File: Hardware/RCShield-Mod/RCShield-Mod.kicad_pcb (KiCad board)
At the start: 2 copper layers, 13 parts, among them K1 PPM_OUT, P1 ANALOG_EXT, P2 DIGI_EXT, P7 Vinput

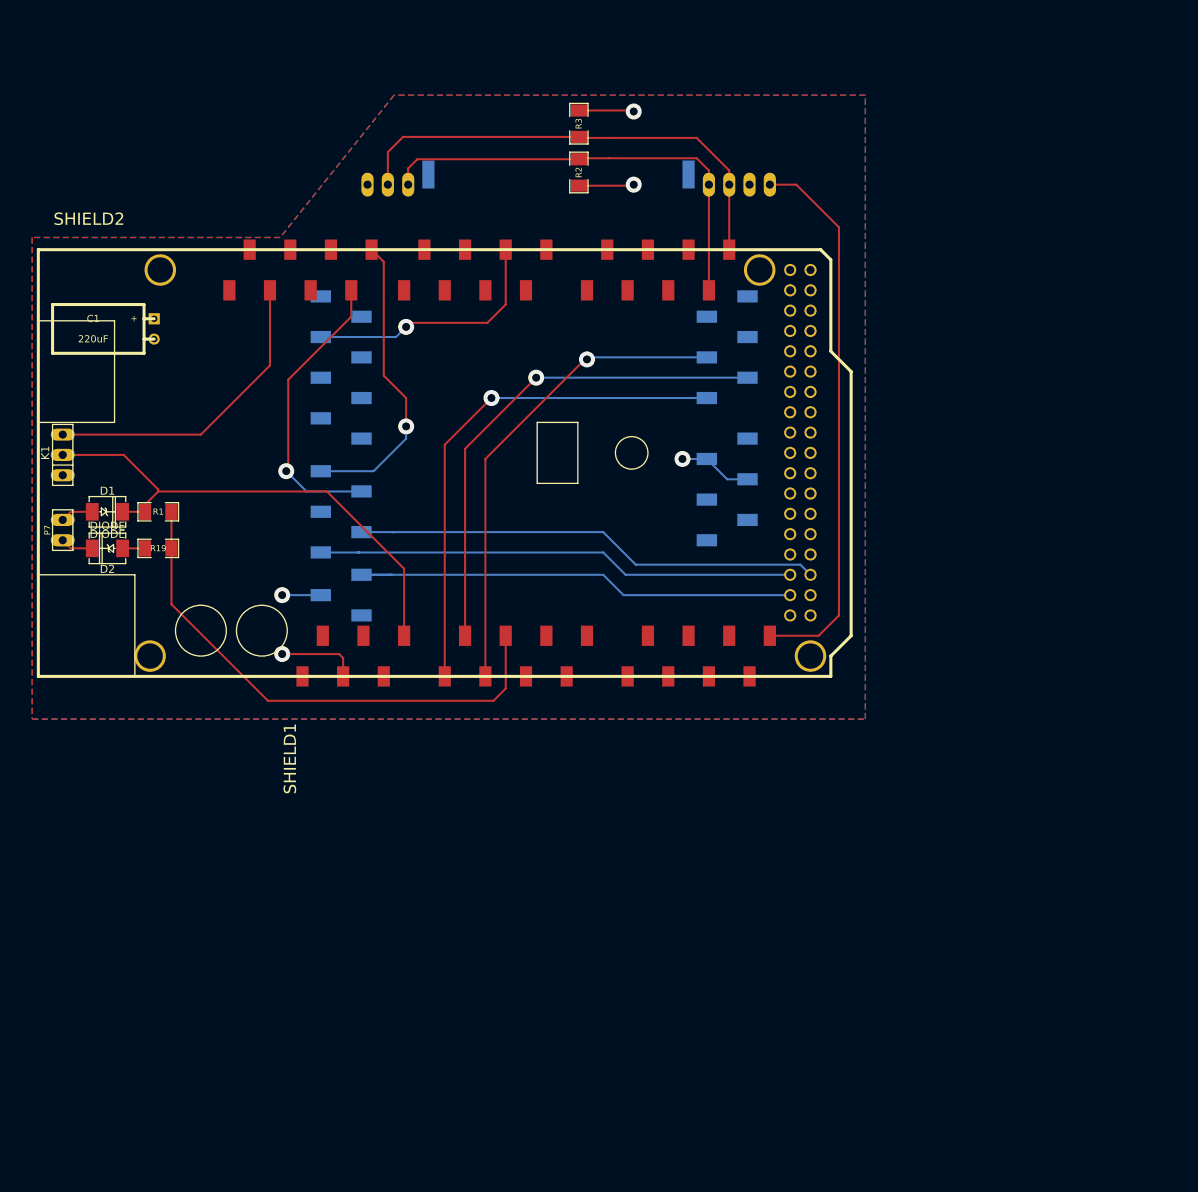
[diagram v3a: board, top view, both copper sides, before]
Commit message: * Updating PCB to more rectangular + Caps + On/Off Switch * Disabling Digital Breakout board for now
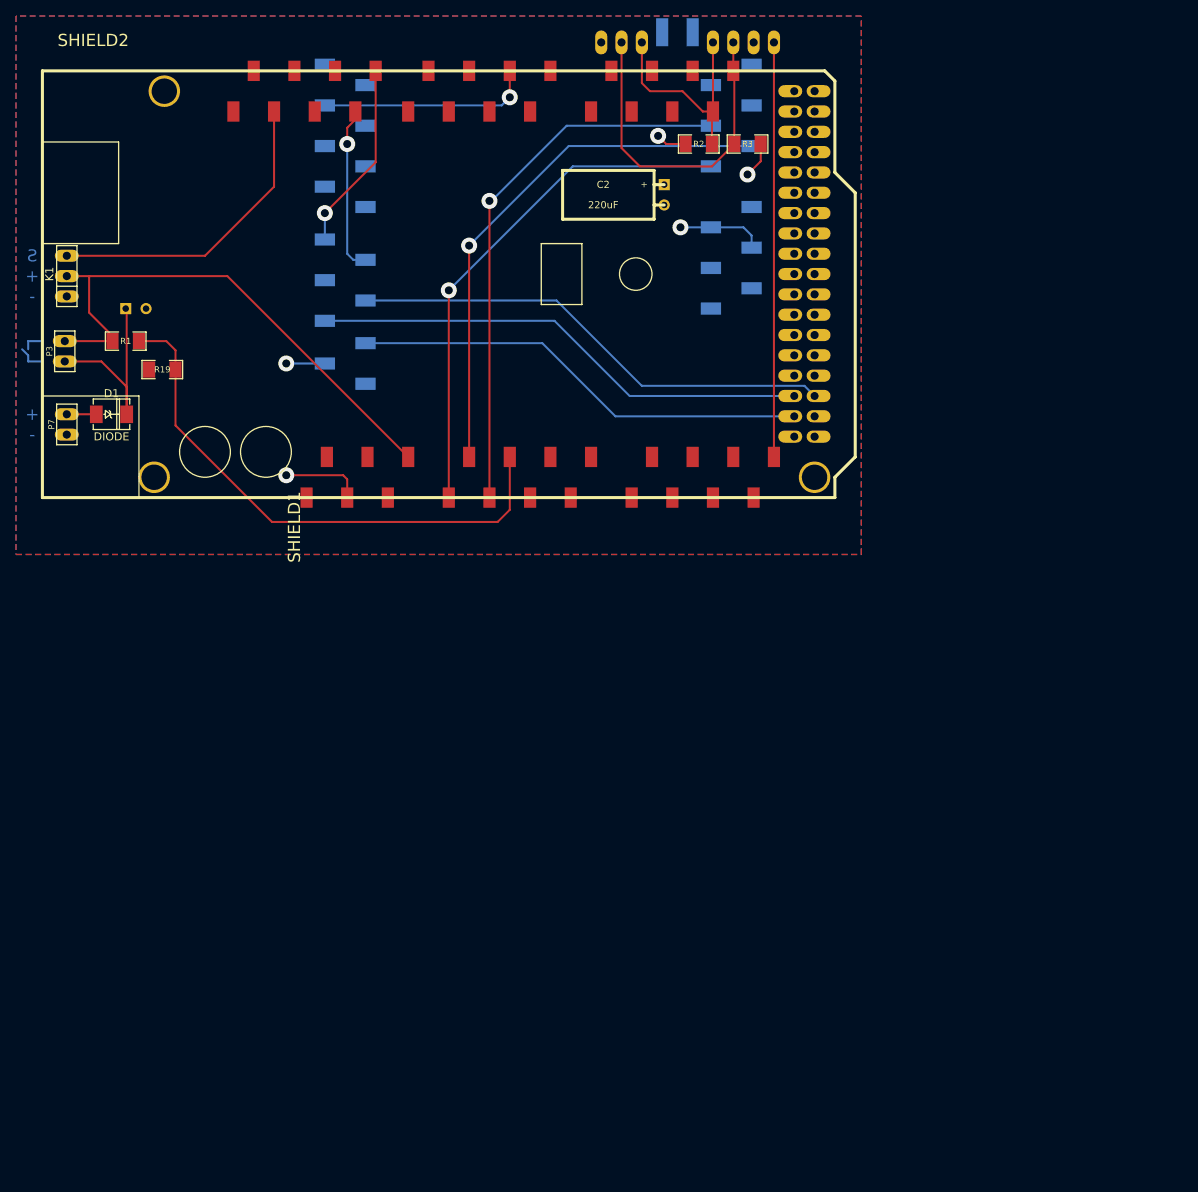
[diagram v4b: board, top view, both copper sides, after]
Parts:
- removed D2: DIODE, DO-214AC(SMA)
- added C2: 220uF, C1V5H, F.Cu at (102.9, 42.9)
- added P3: Vswitch, PIN_ARRAY_2X1_BIG, F.Cu at (27.9, 62.5)
- C1: value 220uF -> 1000uF; moved to B.Cu
- moved P1 34.2 mm to (98.8, 23.9)
- moved SHIELD1 29.0 mm to (113.8, 90.2)
- moved K1 22.4 mm to (28.2, 53.1)
- moved R19 22.4 mm to (40.1, 64.8)
- moved SHIELD2 22.4 mm to (25.1, 80.8)
- moved R1 21.7 mm to (35.6, 61.2)
- moved R3 21.2 mm to (113.3, 36.6), turned to 180 degrees
- moved P2 17.8 mm to (111.5, 23.9)
- moved R2 15.4 mm to (107.2, 36.6), turned to 0 degrees
- moved P7 13.2 mm to (28.2, 71.6)
- moved D1 12.2 mm to (33.8, 70.4)
- moved C1 3.42 mm to (36.8, 57.1), turned to 0 degrees
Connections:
- C1 pad 1: +5V -> Valways
- D1 pad 2: VIN -> Valways
- P7 pad 1: N-0000017 -> GND
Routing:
- net SDA: track 55.8 -> 28.2 mm
- net Valways: track 0.00 -> 25.7 mm
- net DIGI_INT: track 69.0 -> 51.8 mm
- net SCL: track 59.2 -> 42.2 mm
- net SDSEL: track 36.4 -> 20.8 mm
- net GPUSEL: track 37.8 -> 23.7 mm
- net ACCZ: track 60.1 -> 68.7 mm
- net (no net): track 0.00 -> 6.41 mm
- net +5V: track 23.9 -> 18.5 mm
- net DISPINT: track 31.7 -> 26.8 mm
- net ACCY: track 62.4 -> 66.9 mm
- net VIN: track 63.1 -> 67.3 mm
- net N-0000017: track 4.11 -> 0.00 mm
- net Vsense: track 65.6 -> 68.5 mm
- net MISO: track 60.1 -> 62.6 mm
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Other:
- board text added: "+"
- board text added: "-"
- board text added: "S"
